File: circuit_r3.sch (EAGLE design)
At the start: 24 parts, among them IC1 7805DT, U1 MCP4725, U2 MB85RC256VPF-G-JNERE2, U4 ATMEGA328P_VQFNVQFN, Y1 16MHz

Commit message: Oooh, getting close.
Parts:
- removed C7: 0.1uF, custom:C
- added J1: (no value), SparkFun-Connectors:6_PIN_SERIAL_TARGETSILK
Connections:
- removed net AREF: C7.1, U4.AREF
- new net RXI: J1.TXO, U4.PD0(RXD)
- new net TXO: J1.RXI, U4.PD1(TXD)
- net DTR: now also J1.DTR
- net GND: now also J1.CTS, J1.GND; no longer C7.2
- net VCC: now also J1.VCC
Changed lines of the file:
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@@
 </variantdefs>
 <classes>
-<class number="0" name="default" width="0.254" drill="0">
+<class number="0" name="default" width="0.1524" drill="0">
 <clearance class="0" value="0.205"/>
 </class>
@@
 <part name="C5" library="custom" deviceset="C" device="" value="0.1uF"/>
 <part name="C6" library="custom" deviceset="C" device="" value="0.1uF"/>
-<part name="C7" library="custom" deviceset="C" device="" value="0.1uF"/>
 <part name="U4" library="SparkFun-IC-Microcontroller" deviceset="ATMEGA328P_VQFN" device="VQFN"/>
 <part name="R6" library="adafruit" library_urn="urn:adsk.eagle:library:420" deviceset="R-US_" device="R0603" package3d_urn="urn:adsk.eagle:package:6240565/1" value="1M"/>
 <part name="Y1" library="SparkFun-Clocks" deviceset="CRYSTAL-16MHZ" device="SMD-5X3.2" value="16MHz"/>
+<part name="J1" library="SparkFun-Connectors" deviceset="6_PIN_SERIAL_TARGET" device="SILK"/>
 </parts>
 <sheets>
@@
 <attribute name="VALUE" x="103.378" y="10.795" size="1.778" layer="96" font="vector"/>
 </instance>
-<instance part="C7" gate="C" x="-96.52" y="8.89" smashed="yes">
-<attribute name="NAME" x="-93.472" y="12.573" size="1.778" layer="95" font="vector" rot="R180"/>
-<attribute name="VALUE" x="-94.742" y="5.715" size="1.778" layer="96" font="vector"/>
-</instance>
 <instance part="U4" gate="U1" x="-68.58" y="22.86" smashed="yes">
 <attribute name="NAME" x="-86.36" y="56.642" size="1.778" layer="95"/>
@@
 <attribute name="NAME" x="-112.776" y="25.908" size="1.778" layer="95" font="vector" rot="R90" align="bottom-center"/>
 <attribute name="VALUE" x="-108.712" y="25.908" size="1.778" layer="96" font="vector" rot="R90" align="top-center"/>
+</instance>
+<instance part="J1" gate="G$1" x="-7.62" y="132.08" smashed="yes">
+<attribute name="VALUE" x="-15.24" y="122.174" size="1.778" layer="96" font="vector"/>
+<attribute name="NAME" x="-15.24" y="142.748" size="1.778" layer="95" font="vector"/>
 </instance>
 </instances>
@@
 </segment>
 <segment>
-<pinref part="C7" gate="C" pin="2"/>
 <pinref part="GND9" gate="1" pin="GND"/>
-<wire x1="-96.52" y1="5.08" x2="-96.52" y2="-2.54" width="0.1524" layer="91"/>
 <pinref part="U4" gate="U1" pin="GND"/>
 <wire x1="-96.52" y1="-2.54" x2="-96.52" y2="-5.08" width="0.1524" layer="91"/>
 <wire x1="-96.52" y1="-5.08" x2="-96.52" y2="-7.874" width="0.1524" layer="91"/>
 <wire x1="-88.9" y1="-2.54" x2="-96.52" y2="-2.54" width="0.1524" layer="91"/>
-<junction x="-96.52" y="-2.54"/>
 <pinref part="U4" gate="U1" pin="GND@PAD"/>
 <wire x1="-88.9" y1="-5.08" x2="-96.52" y2="-5.08" width="0.1524" layer="91"/>
 <junction x="-96.52" y="-5.08"/>
+</segment>
+<segment>
+<pinref part="J1" gate="G$1" pin="GND"/>
+<wire x1="-2.54" y1="139.7" x2="2.54" y2="139.7" width="0.1524" layer="91"/>
+<label x="-2.54" y="139.7" size="1.778" layer="95"/>
+</segment>
+<segment>
+<pinref part="J1" gate="G$1" pin="CTS"/>
+<wire x1="-2.54" y1="137.16" x2="2.54" y2="137.16" width="0.1524" layer="91"/>
+<label x="-2.54" y="137.16" size="1.778" layer="95"/>
 </segment>
 </net>
@@
 <pinref part="P+8" gate="VCC" pin="VCC"/>
 <pinref part="R5" gate="G$1" pin="2"/>
+</segment>
+<segment>
+<pinref part="J1" gate="G$1" pin="VCC"/>
+<wire x1="-2.54" y1="134.62" x2="2.54" y2="134.62" width="0.1524" layer="91"/>
+<label x="-2.54" y="134.62" size="1.778" layer="95"/>
 </segment>
 </net>
@@
 <label x="-121.92" y="60.96" size="1.778" layer="95"/>
 </segment>
-</net>
-<net name="AREF" class="0">
-<segment>
-<pinref part="U4" gate="U1" pin="AREF"/>
-<wire x1="-88.9" y1="38.1" x2="-96.52" y2="38.1" width="0.1524" layer="91"/>
-<pinref part="C7" gate="C" pin="1"/>
-<wire x1="-96.52" y1="38.1" x2="-96.52" y2="12.7" width="0.1524" layer="91"/>
-<label x="-96.52" y="38.1" size="1.778" layer="95"/>
+<segment>
+<pinref part="J1" gate="G$1" pin="DTR"/>
+<wire x1="-2.54" y1="127" x2="2.54" y2="127" width="0.1524" layer="91"/>
+<label x="-2.54" y="127" size="1.778" layer="95"/>
 </segment>
 </net>
@@
 </segment>
 </net>
+<net name="RXI" class="0">
+<segment>
+<pinref part="U4" gate="U1" pin="PD0(RXD)"/>
+<wire x1="-45.72" y1="30.48" x2="-40.64" y2="30.48" width="0.1524" layer="91"/>
+<label x="-43.18" y="30.48" size="1.778" layer="95"/>
+</segment>
+<segment>
+<pinref part="J1" gate="G$1" pin="TXO"/>
+<wire x1="-2.54" y1="132.08" x2="2.54" y2="132.08" width="0.1524" layer="91"/>
+<label x="-2.54" y="132.08" size="1.778" layer="95"/>
+</segment>
+</net>
+<net name="TXO" class="0">
+<segment>
+<pinref part="U4" gate="U1" pin="PD1(TXD)"/>
+<wire x1="-45.72" y1="27.94" x2="-40.64" y2="27.94" width="0.1524" layer="91"/>
+<label x="-43.18" y="27.94" size="1.778" layer="95"/>
+</segment>
+<segment>
+<pinref part="J1" gate="G$1" pin="RXI"/>
+<wire x1="-2.54" y1="129.54" x2="2.54" y2="129.54" width="0.1524" layer="91"/>
+<label x="-2.54" y="129.54" size="1.778" layer="95"/>
+</segment>
+</net>

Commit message: More revisions...
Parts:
- added J2: (no value), SparkFun-Connectors:CONN_03X22X3_SILK_MALE_PTH
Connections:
- new net ISP_MISO: J2.6, U4.PB4(MISO)
- new net ISP_MOSI: J2.3, U4.PB3(MOSI/OC2)
- new net ISP_SCK: J2.4, U4.PB5(SCK)
- net GND: now also J2.1
- net RESET: now also J2.2
- net VCC: now also J2.5
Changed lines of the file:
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@@
 <part name="Y1" library="SparkFun-Clocks" deviceset="CRYSTAL-16MHZ" device="SMD-5X3.2" value="16MHz"/>
 <part name="J1" library="SparkFun-Connectors" deviceset="6_PIN_SERIAL_TARGET" device="SILK"/>
+<part name="J2" library="SparkFun-Connectors" deviceset="CONN_03X2" device="2X3_SILK_MALE_PTH"/>
+<part name="GND4" library="supply1" library_urn="urn:adsk.eagle:library:371" deviceset="GND" device=""/>
 </parts>
 <sheets>
@@
 <attribute name="NAME" x="-15.24" y="142.748" size="1.778" layer="95" font="vector"/>
 </instance>
+<instance part="J2" gate="G$1" x="-30.48" y="-20.32" smashed="yes">
+<attribute name="NAME" x="-34.036" y="-14.732" size="1.778" layer="95" font="vector"/>
+<attribute name="VALUE" x="-33.782" y="-26.162" size="1.778" layer="96" font="vector" align="top-left"/>
+</instance>
+<instance part="GND4" gate="1" x="-53.34" y="-27.94" smashed="yes">
+<attribute name="VALUE" x="-55.88" y="-30.48" size="1.778" layer="96"/>
+</instance>
 </instances>
 <busses>
@@
 <label x="-2.54" y="137.16" size="1.778" layer="95"/>
 </segment>
+<segment>
+<pinref part="J2" gate="G$1" pin="1"/>
+<wire x1="-38.1" y1="-17.78" x2="-53.34" y2="-17.78" width="0.1524" layer="91"/>
+<wire x1="-53.34" y1="-17.78" x2="-53.34" y2="-25.4" width="0.1524" layer="91"/>
+<pinref part="GND4" gate="1" pin="GND"/>
+</segment>
 </net>
 <net name="VCC" class="0">
@@
 <wire x1="-2.54" y1="134.62" x2="2.54" y2="134.62" width="0.1524" layer="91"/>
 <label x="-2.54" y="134.62" size="1.778" layer="95"/>
+</segment>
+<segment>
+<pinref part="J2" gate="G$1" pin="5"/>
+<wire x1="-38.1" y1="-22.86" x2="-40.64" y2="-22.86" width="0.1524" layer="91"/>
+<label x="-43.18" y="-22.86" size="1.778" layer="95"/>
 </segment>
 </net>
@@
 <junction x="-99.06" y="60.96"/>
 </segment>
+<segment>
+<pinref part="J2" gate="G$1" pin="2"/>
+<wire x1="-22.86" y1="-17.78" x2="-20.32" y2="-17.78" width="0.1524" layer="91"/>
+<label x="-22.86" y="-17.78" size="1.778" layer="95"/>
+</segment>
 </net>
 <net name="DTR" class="0">
@@
 </segment>
 </net>
+<net name="ISP_MOSI" class="0">
+<segment>
+<pinref part="J2" gate="G$1" pin="3"/>
+<wire x1="-38.1" y1="-20.32" x2="-40.64" y2="-20.32" width="0.1524" layer="91"/>
+<label x="-50.8" y="-20.32" size="1.778" layer="95"/>
+</segment>
+<segment>
+<pinref part="U4" gate="U1" pin="PB3(MOSI/OC2)"/>
+<wire x1="-45.72" y1="0" x2="-35.56" y2="0" width="0.1524" layer="91"/>
+<label x="-43.18" y="0" size="1.778" layer="95"/>
+</segment>
+</net>
+<net name="ISP_SCK" class="0">
+<segment>
+<pinref part="J2" gate="G$1" pin="4"/>
+<wire x1="-22.86" y1="-20.32" x2="-20.32" y2="-20.32" width="0.1524" layer="91"/>
+<label x="-22.86" y="-20.32" size="1.778" layer="95"/>
+</segment>
+<segment>
+<pinref part="U4" gate="U1" pin="PB5(SCK)"/>
+<wire x1="-45.72" y1="-5.08" x2="-35.56" y2="-5.08" width="0.1524" layer="91"/>
+<label x="-43.18" y="-5.08" size="1.778" layer="95"/>
+</segment>
+</net>
+<net name="ISP_MISO" class="0">
+<segment>
+<pinref part="J2" gate="G$1" pin="6"/>
+<wire x1="-22.86" y1="-22.86" x2="-20.32" y2="-22.86" width="0.1524" layer="91"/>
+<label x="-22.86" y="-22.86" size="1.778" layer="95"/>
+</segment>
+<segment>
+<pinref part="U4" gate="U1" pin="PB4(MISO)"/>
+<wire x1="-45.72" y1="-2.54" x2="-35.56" y2="-2.54" width="0.1524" layer="91"/>
+<label x="-43.18" y="-2.54" size="1.778" layer="95"/>
+</segment>
+</net>

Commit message: Pretty good design.
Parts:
- added L_PGM: GREEN, SparkFun-LED:LED-RED0603
- added L_PWR: RED, SparkFun-LED:LED-RED0603
- added L_SNS: BLUE, SparkFun-LED:LED-RED0603
- added R7, R8: 10k, adafruit:R-US_R0603
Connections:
- new net LED_GND: L_PGM.C, L_PWR.C, R8.1
- new net N$2: L_SNS.C, R7.2
- new net SENS_IND: L_SNS.A, U4.PD3(INT1)
- net GND: now also R7.1, R8.2
- net ISP_SCK: now also L_PGM.A
- net VCC: now also L_PWR.A
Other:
- moved on the sheet: 12V, C6, ECU, ETH, ETH_GND, ETH_PWR, GND, IC1, J1, J2, R1

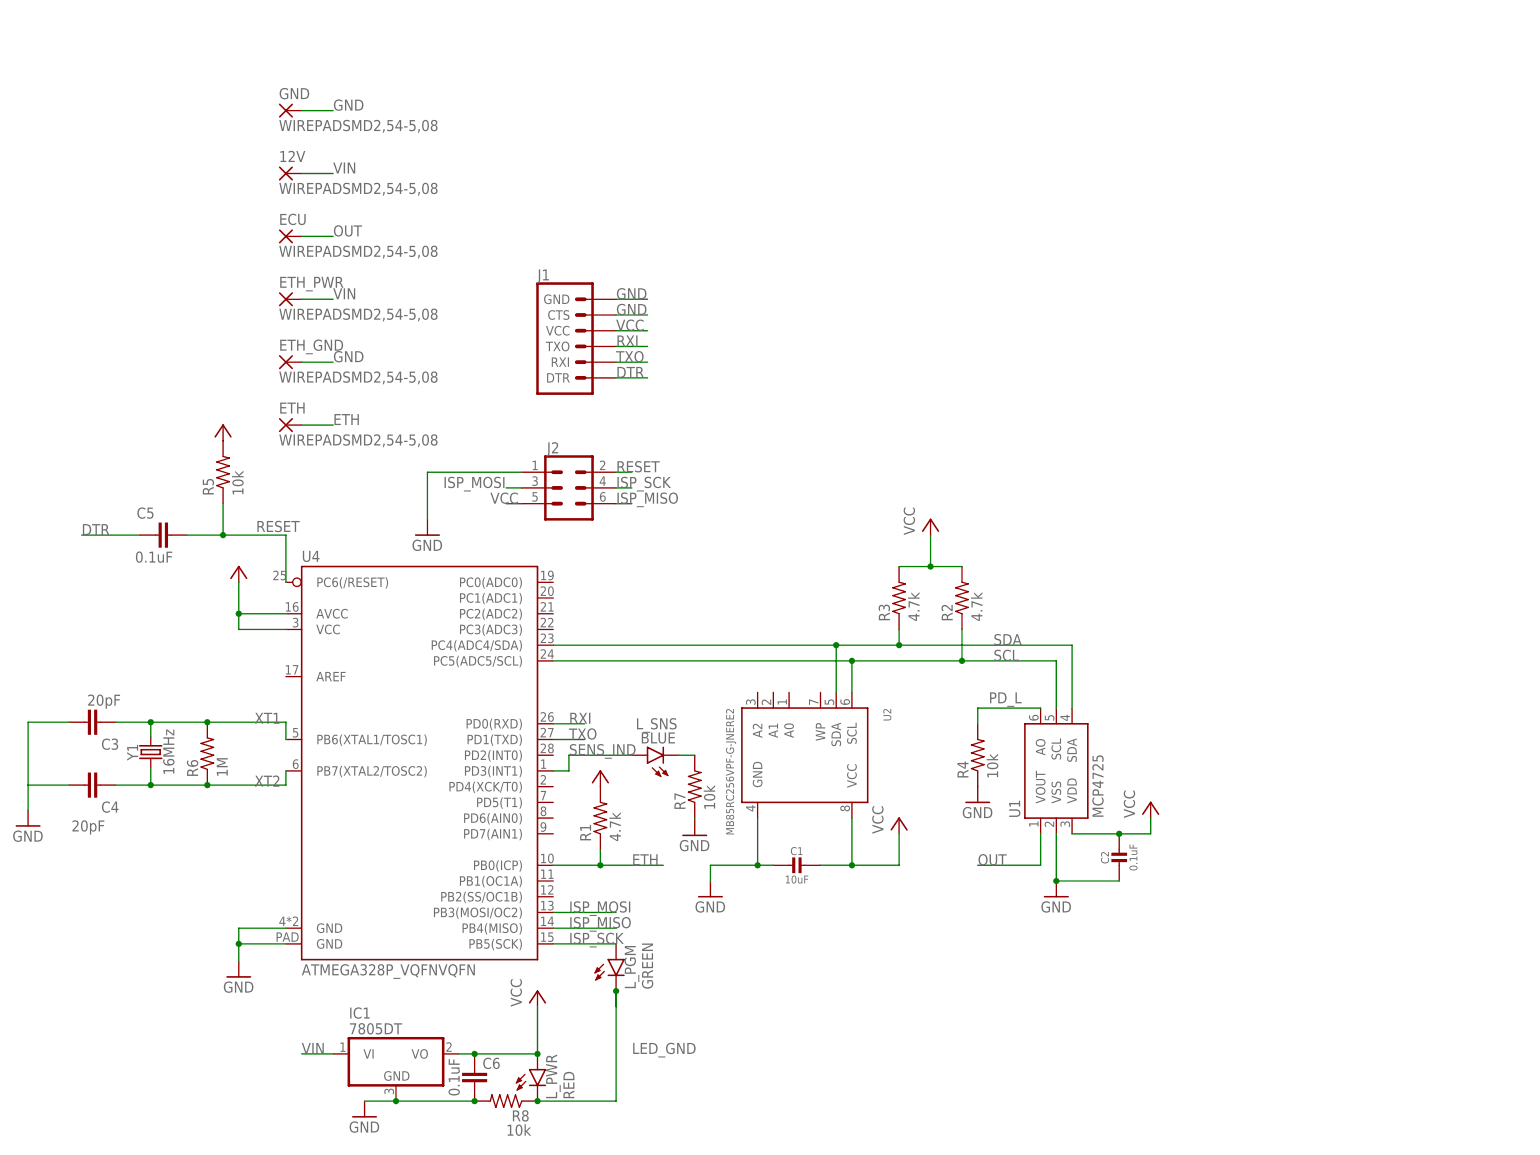
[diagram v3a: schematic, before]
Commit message: Production prototype, including indicator leds.
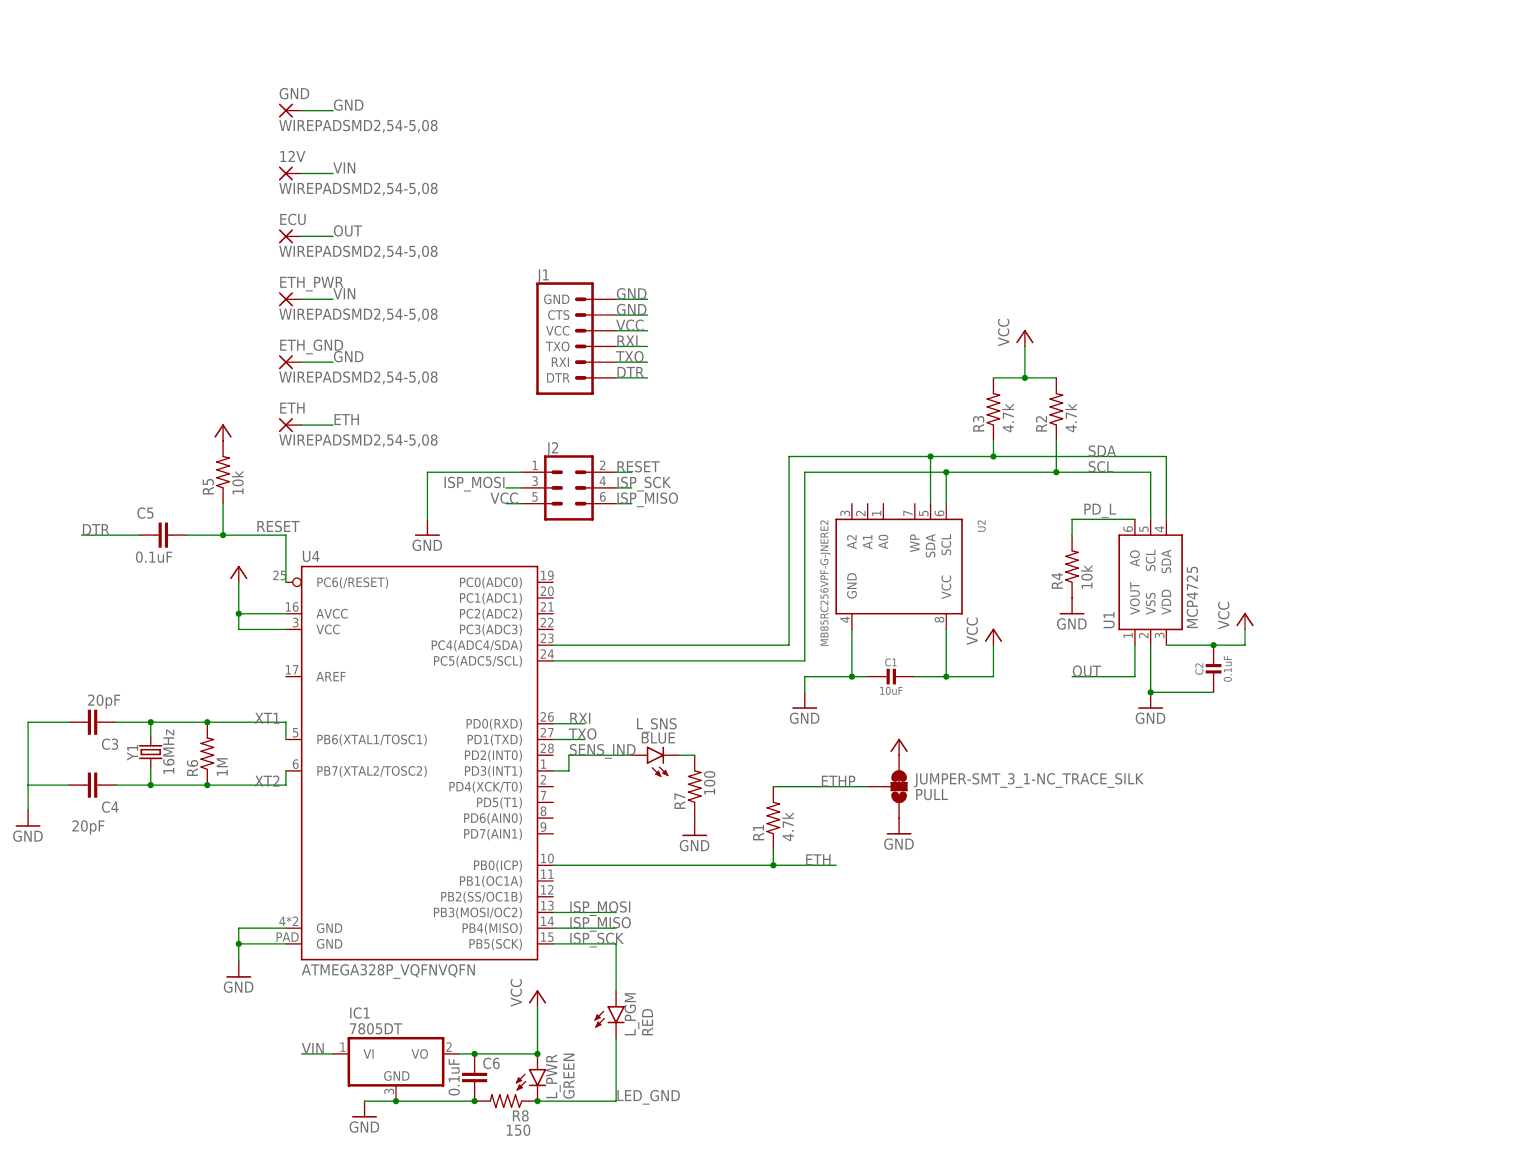
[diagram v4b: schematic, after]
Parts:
- added PULL: JUMPER-SMT_3_1-NC_TRACE_SILK, SparkFun-Jumpers:JUMPER-SMT_3_1-NC_TRACE_SILK
- L_PGM: value GREEN -> RED
- L_PWR: value RED -> GREEN
- R7: value 10k -> 100
- R8: value 10k -> 150
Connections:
- new net ETHP: PULL.2, R1.2
- net GND: now also PULL.1
- net VCC: now also PULL.3; no longer R1.2
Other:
- moved on the sheet: C1, C2, L_PGM, R1, R2, R3, R4, U1, U2
